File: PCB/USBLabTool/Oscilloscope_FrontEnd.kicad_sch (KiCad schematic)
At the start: 92 parts, among them J10 T_pwm, J12 T_buf, J14 ADC1, J15 ADC2, J16 +3.3VA, J4 T_att, J5 T_acdc, J6 T_acdc, J8 T_amp, J9 T_amp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

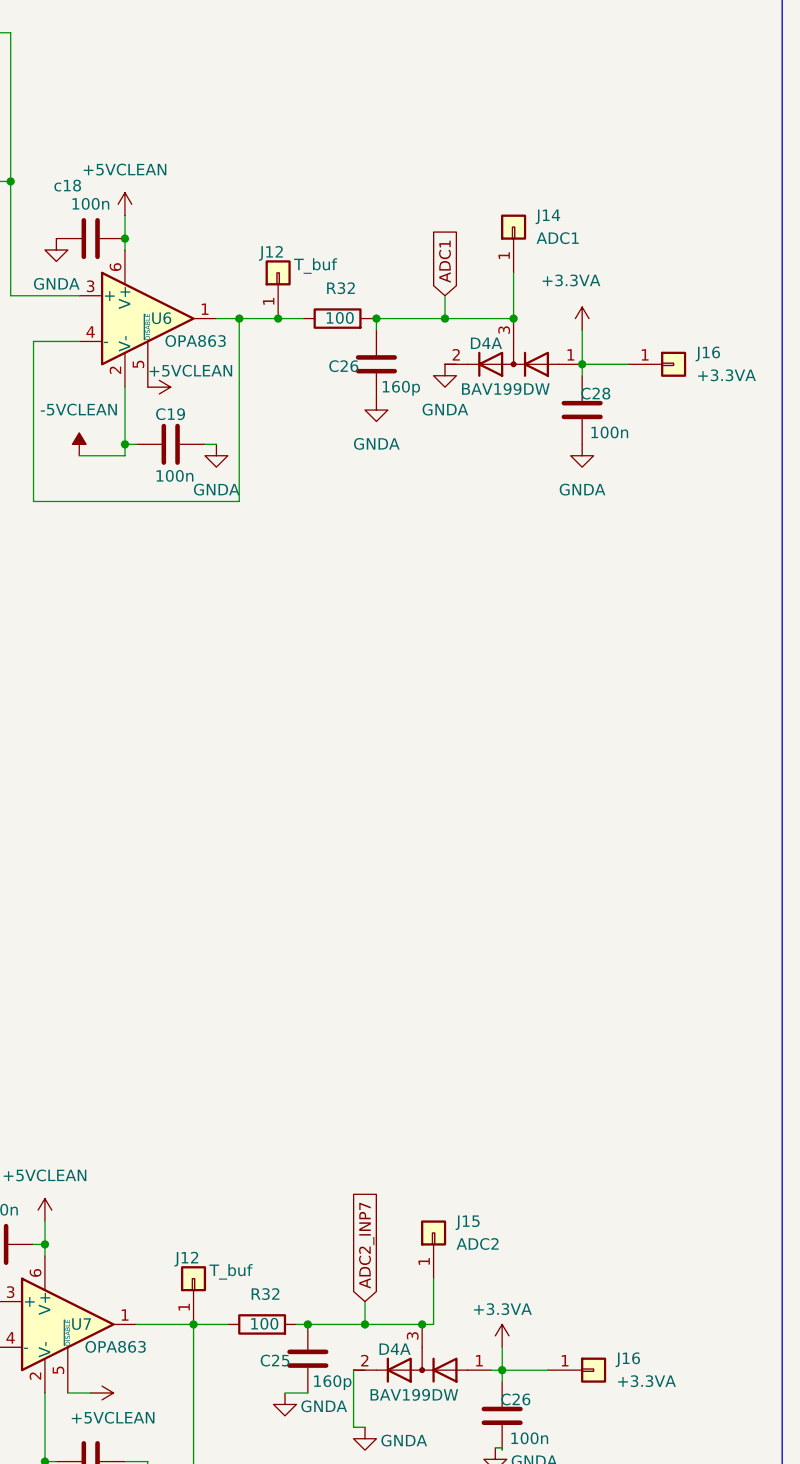
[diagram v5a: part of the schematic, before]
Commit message: rearrange logic pins, connectors, fix some name tags
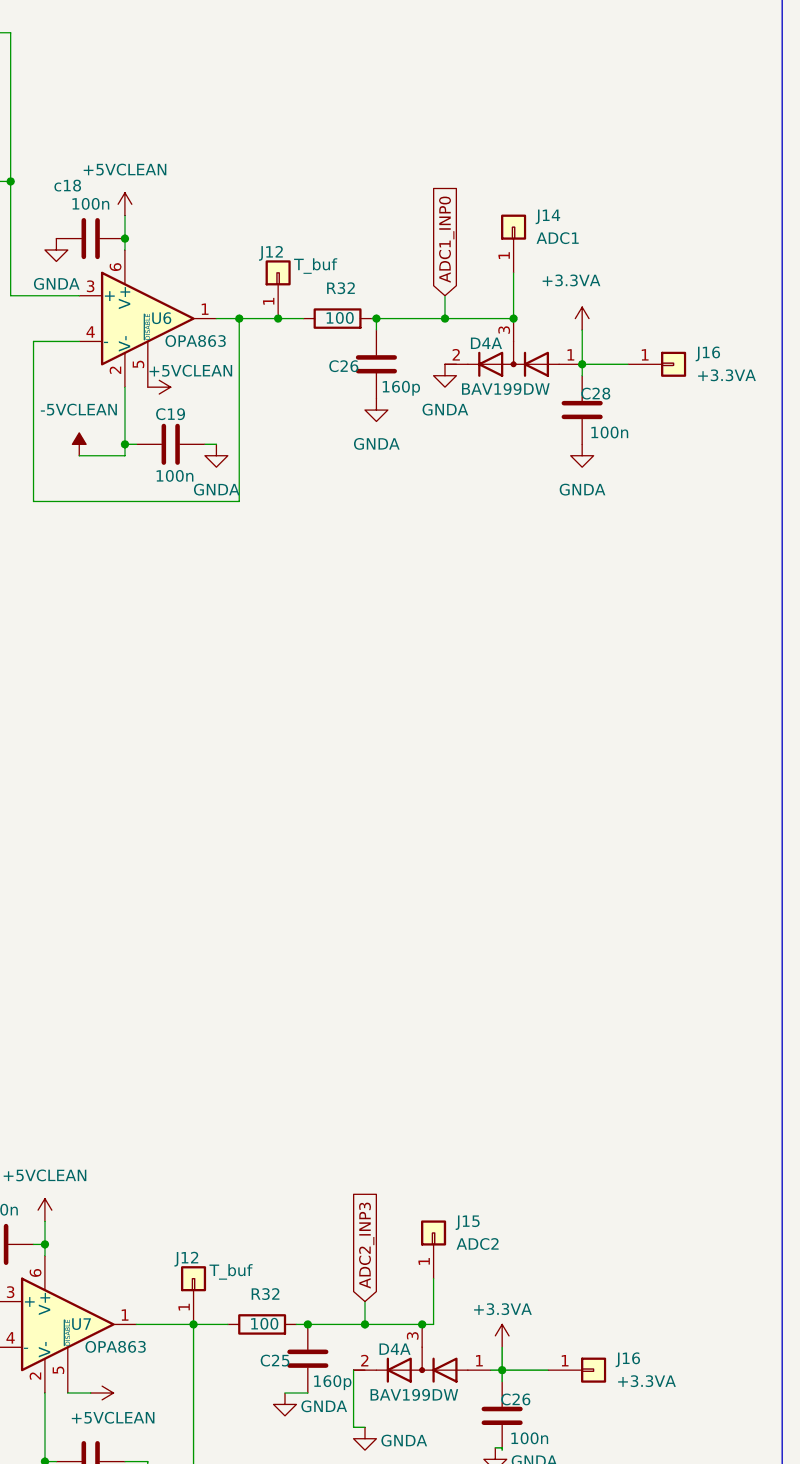
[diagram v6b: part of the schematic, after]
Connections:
- net ADC1 renamed ADC1_INP0
- net ADC2_INP7 renamed ADC2_INP3
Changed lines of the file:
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@@
+		)
+	)
+	(global_label "ADC1_INP0"
+		(shape input)
+		(at 297.18 55.88 90)
+		(fields_autoplaced yes)
+		(effects
+			(font
+				(size 1.27 1.27)
+			)
+			(justify left)
+		)
+		(property "Intersheetrefs" "${INTERSHEET_REFS}"
+			(at 297.18 42.6743 90)
+			(effects
+				(font
+					(size 1.27 1.27)
+				)
+				(justify left)
+				(hide yes)
+			)
 		)
 	)
@@
 		)
 	)
-	(global_label "ADC2_INP7"
+	(global_label "ADC2_INP3"
 		(shape input)
 		(at 288.29 167.64 90)
@@
 				(hide yes)
 			)
-		)
-	)
-	(global_label "ADC1"
-		(shape input)
-		(at 297.18 55.88 90)
-		(fields_autoplaced yes)
-		(effects
-			(font
-				(size 1.27 1.27)
-			)
-			(justify left)
-		)
-		(property "Intersheetrefs" "${INTERSHEET_REFS}"
-			(at 297.18 48.0567 90)
-			(effects
-				(font
-					(size 1.27 1.27)
-				)
-				(justify left)
-				(hide yes)
-			)

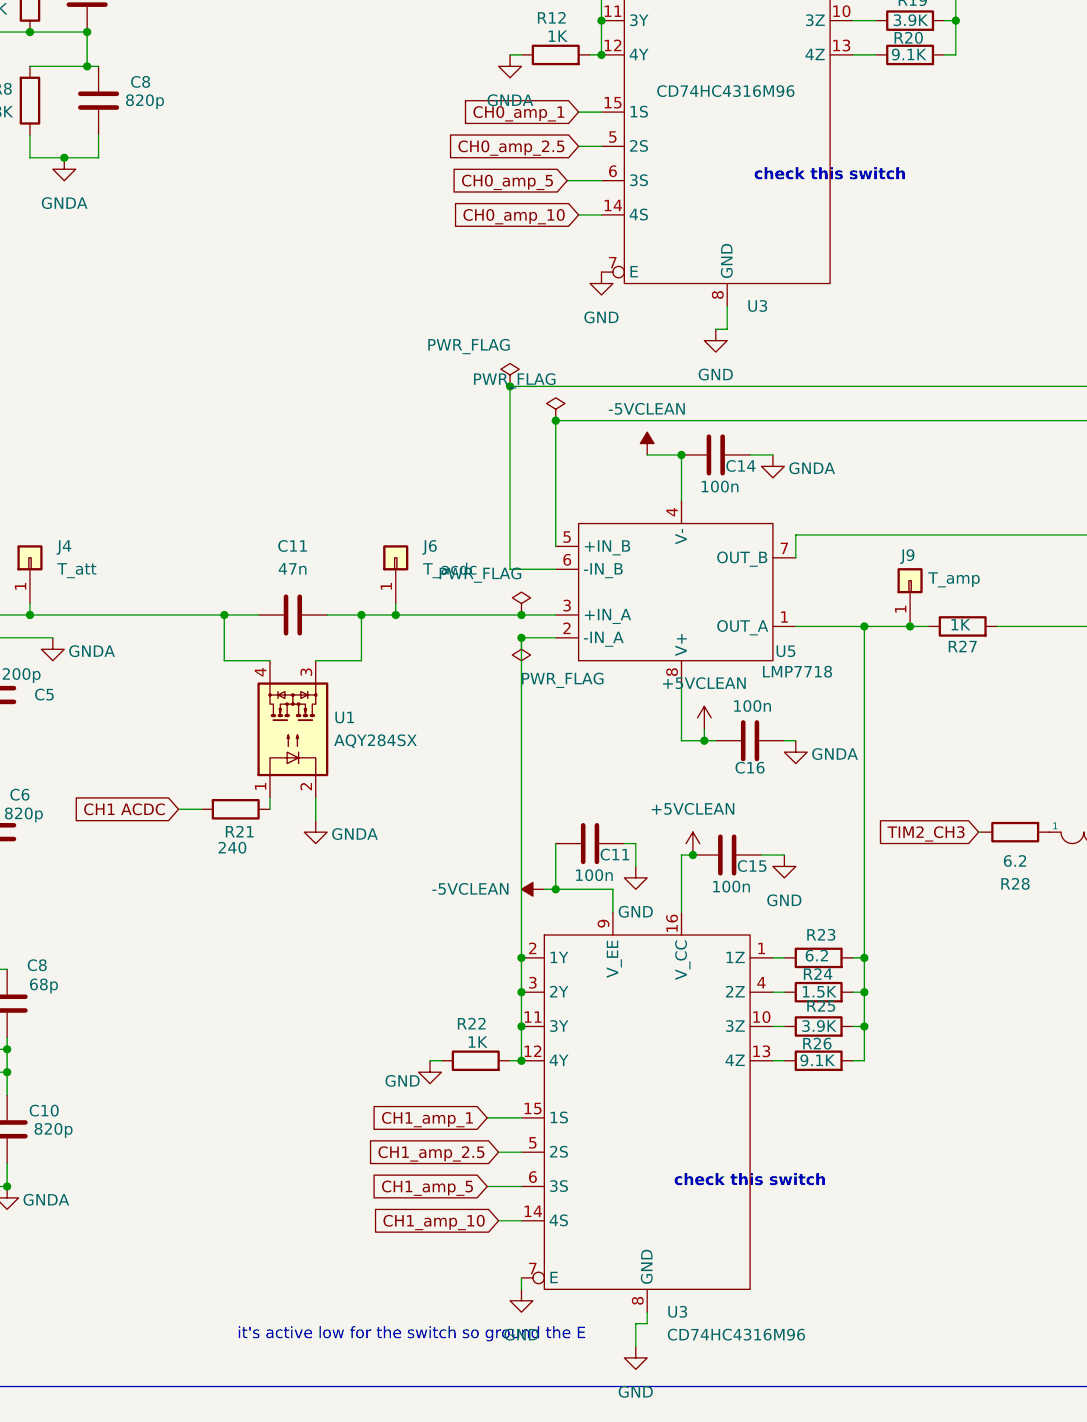
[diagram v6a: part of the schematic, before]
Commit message: Updated schematic and PCB
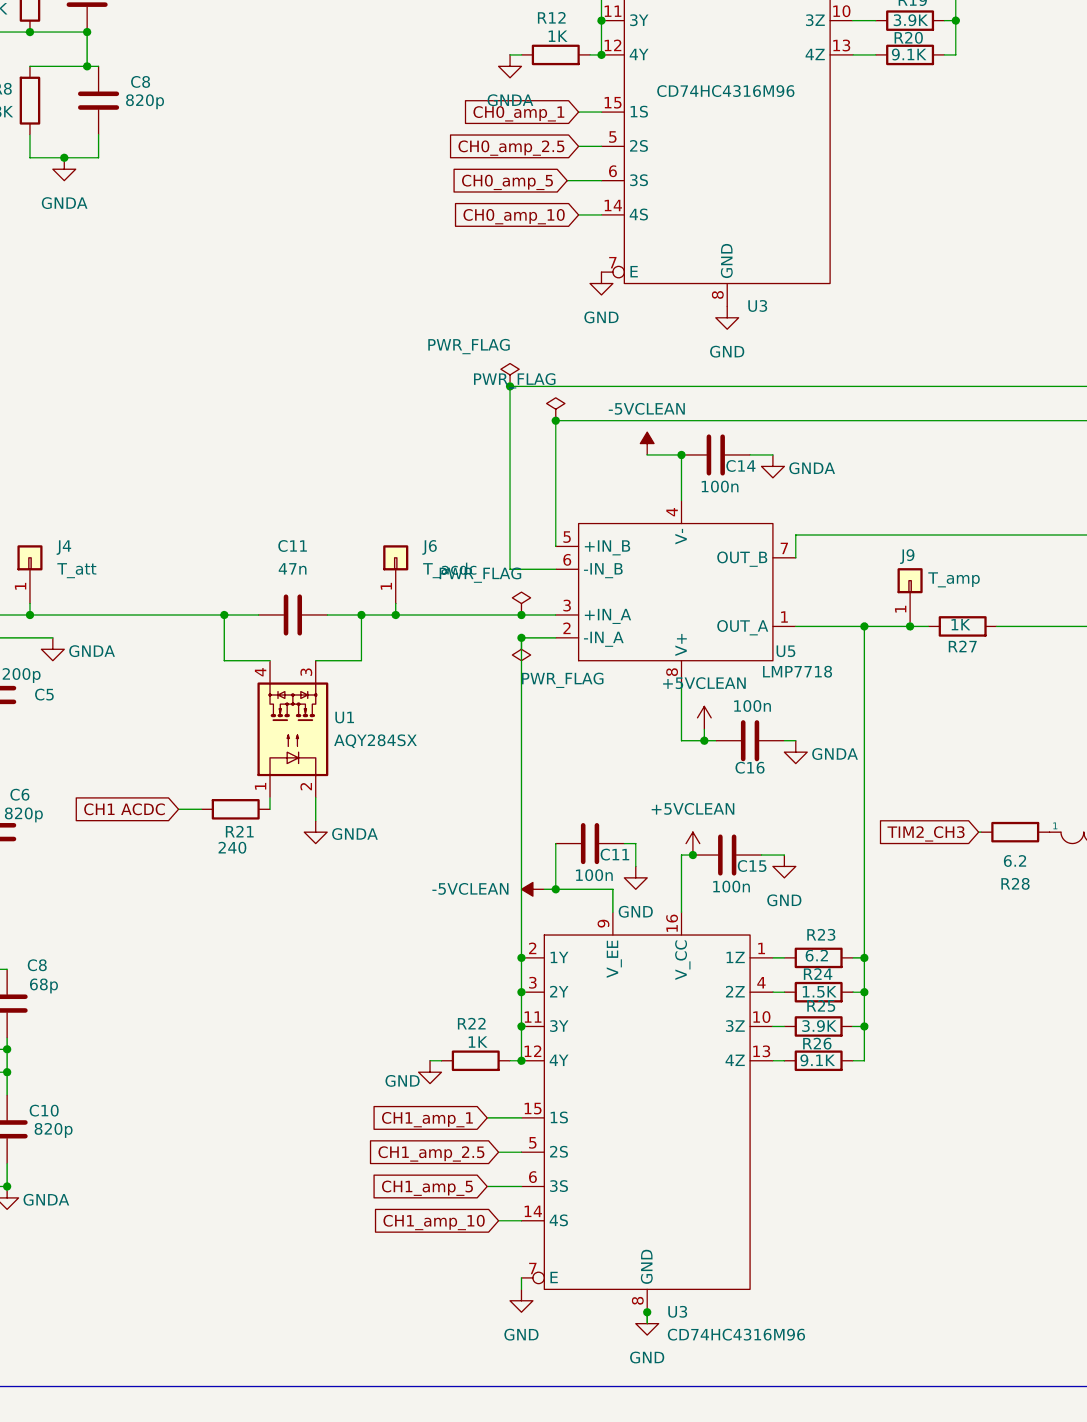
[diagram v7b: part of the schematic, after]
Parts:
- U3: footprint Package_SO:SOIC-16_3.9x9.9mm_P1.27mm -> Package_SO:TSSOP-16_4.4x5mm_P0.65mm
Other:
- note removed: "check this switch"
- note removed: "it's active low for the switch so ground the E"
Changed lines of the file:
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@@
 	)
 	(junction
+		(at 162.56 241.3)
+		(diameter 0)
+		(color 0 0 0 0)
+	)
+	(junction
 		(at 157.48 101.6)
 		(diameter 0)
@@
 	(wire
 		(pts
-			(xy 162.56 242.57) (xy 162.56 241.3)
-		)
-		(stroke
-			(width 0)
-			(type default)
-		)
-	)
-	(wire
-		(pts
 			(xy 81.28 76.2) (xy 81.28 71.12)
 		)
@@
 	(wire
 		(pts
-			(xy 171.45 132.08) (xy 171.45 129.54)
-		)
-		(stroke
-			(width 0)
-			(type default)
-		)
-	)
-	(wire
-		(pts
 			(xy 185.42 93.98) (xy 187.96 93.98)
 		)
@@
 	(wire
 		(pts
-			(xy 161.29 242.57) (xy 162.56 242.57)
-		)
-		(stroke
-			(width 0)
-			(type default)
-		)
-	)
-	(wire
-		(pts
 			(xy 240.03 138.43) (xy 240.03 154.94)
 		)
@@
 	(wire
 		(pts
-			(xy 170.18 132.08) (xy 171.45 132.08)
-		)
-		(stroke
-			(width 0)
-			(type default)
-		)
-	)
-	(wire
-		(pts
 			(xy 237.49 138.43) (xy 240.03 138.43)
 		)
@@
 	(wire
 		(pts
-			(xy 161.29 242.57) (xy 161.29 245.11)
+			(xy 162.56 242.57) (xy 162.56 241.3)
 		)
 		(stroke
@@
 		)
 	)
-	(text "it's active low for the switch so ground the E\n"
-		(exclude_from_sim no)
-		(at 136.398 243.84 0)
-		(effects
-			(font
-				(size 1.27 1.27)
-			)
-		)
-	)
 	(text "SCOPE CHAN 1"
 		(exclude_from_sim no)
@@
 		)
 	)
-	(text "check this switch"
-		(exclude_from_sim no)
-		(at 182.88 115.062 0)
-		(effects
-			(font
-				(size 1.27 1.27)
-				(thickness 0.254)
-				(bold yes)
-			)
-		)
-	)
-	(text "check this switch"
-		(exclude_from_sim no)
-		(at 173.99 226.822 0)
-		(effects
-			(font
-				(size 1.27 1.27)
-				(thickness 0.254)
-				(bold yes)
-			)
-		)
-	)
 	(global_label "CH1_amp_1"
 		(shape input)
@@
 		(lib_name "GND_5")
 		(lib_id "power:GND")
-		(at 161.29 245.11 0)
+		(at 162.56 241.3 0)
 		(unit 1)
 		(exclude_from_sim no)
@@
 		(fields_autoplaced yes)
 		(property "Reference" "#PWR018"
-			(at 161.29 251.46 0)
+			(at 162.56 247.65 0)
 			(effects
 				(font
@@
 		)
 		(property "Value" "GND"
-			(at 161.29 250.19 0)
+			(at 162.56 246.38 0)
 			(effects
 				(font
@@
 		)
 		(property "Footprint" ""
-			(at 161.29 245.11 0)
+			(at 162.56 241.3 0)
 			(effects
 				(font
@@
 		)
 		(property "Datasheet" ""
-			(at 161.29 245.11 0)
+			(at 162.56 241.3 0)
 			(effects
 				(font
@@
 		)
 		(property "Description" ""
-			(at 161.29 245.11 0)
+			(at 162.56 241.3 0)
 			(effects
 				(font
@@
 		(lib_name "GND_4")
 		(lib_id "power:GND")
-		(at 170.18 132.08 0)
+		(at 171.45 129.54 0)
 		(unit 1)
 		(exclude_from_sim no)
@@
 		(fields_autoplaced yes)
 		(property "Reference" "#PWR024"
-			(at 170.18 138.43 0)
+			(at 171.45 135.89 0)
 			(effects
 				(font
@@
 		)
 		(property "Value" "GND"
-			(at 170.18 137.16 0)
+			(at 171.45 134.62 0)
 			(effects
 				(font
@@
 		)
 		(property "Footprint" ""
-			(at 170.18 132.08 0)
+			(at 171.45 129.54 0)
 			(effects
 				(font
@@
 		)
 		(property "Datasheet" ""
-			(at 170.18 132.08 0)
+			(at 171.45 129.54 0)
 			(effects
 				(font
@@
 		)
 		(property "Description" ""
-			(at 170.18 132.08 0)
+			(at 171.45 129.54 0)
 			(effects
 				(font
@@
 			)
 		)
-		(property "Footprint" "Package_SO:SOIC-16_3.9x9.9mm_P1.27mm"
+		(property "Footprint" "Package_SO:TSSOP-16_4.4x5mm_P0.65mm"
 			(at 149.86 198.12 0)
 			(effects
@@
 			)
 		)
-		(property "Footprint" "Package_SO:SOIC-16_3.9x9.9mm_P1.27mm"
+		(property "Footprint" "Package_SO:TSSOP-16_4.4x5mm_P0.65mm"
 			(at 158.75 86.36 0)
 			(effects
